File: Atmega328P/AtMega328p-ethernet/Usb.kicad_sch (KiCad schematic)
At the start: 19 parts, among them J2 USB_C_Receptacle_USB2.0_16P, U3 MCP2200-I-SS, Y3 12MHz

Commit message: Most components selected using lcsc
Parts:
- removed C25: 100nF, Capacitor_SMD:C_0603_1608Metric, symbol Device:C_Small
- removed R20: 470R, Resistor_SMD:R_0603_1608Metric, symbol Device:R_Small
- removed U3: MCP2200-I-SS, Package_SO:SSOP-20_5.3x7.2mm_P0.65mm, symbol Interface_USB:MCP2200-I-SS
- added U3: CP2102N-Axx-xQFN28, Package_DFN_QFN:QFN-28-1EP_5x5mm_P0.5mm_EP3.35x3.35mm, symbol Interface_USB:CP2102N-Axx-xQFN28
- D3: value LED -> LED-GREEN; footprint LED_SMD:LED_0603_1608Metric -> LED_SMD:LED_0805_2012Metric; LCSC C2286 -> C2297
- FB2: value HH-1M1608-121JT -> 100R@100MHz; LCSC (none) -> C1015
- J2: value USB_C_Receptacle_USB2.0_16P -> USB_C_Receptacle_USB2.0_12P; LCSC (none) -> C2988369
- R21: value 10k -> 1k
- Y3: footprint Crystal:Crystal_SMD_2012-2Pin_2.0x1.2mm -> Crystal:Crystal_SMD_3225-4Pin_3.2x2.5mm
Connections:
- net USB_P is gone; now on net USB_N: J2.A6 (D+), J2.B6 (D+)
- net +5V: now also U3.6 (VDD)
- net USB_N: now also U3.4 (D+), U3.5 (D-)
- net VBUS: now also U3.8 (VBUS)
- new net: U3.29 (GND), U3.3 (GND)
- no-connect marks 5 -> 4
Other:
- moved on the sheet: C26, C27, FB2, R21, TP1, TP2, TP3, TP4

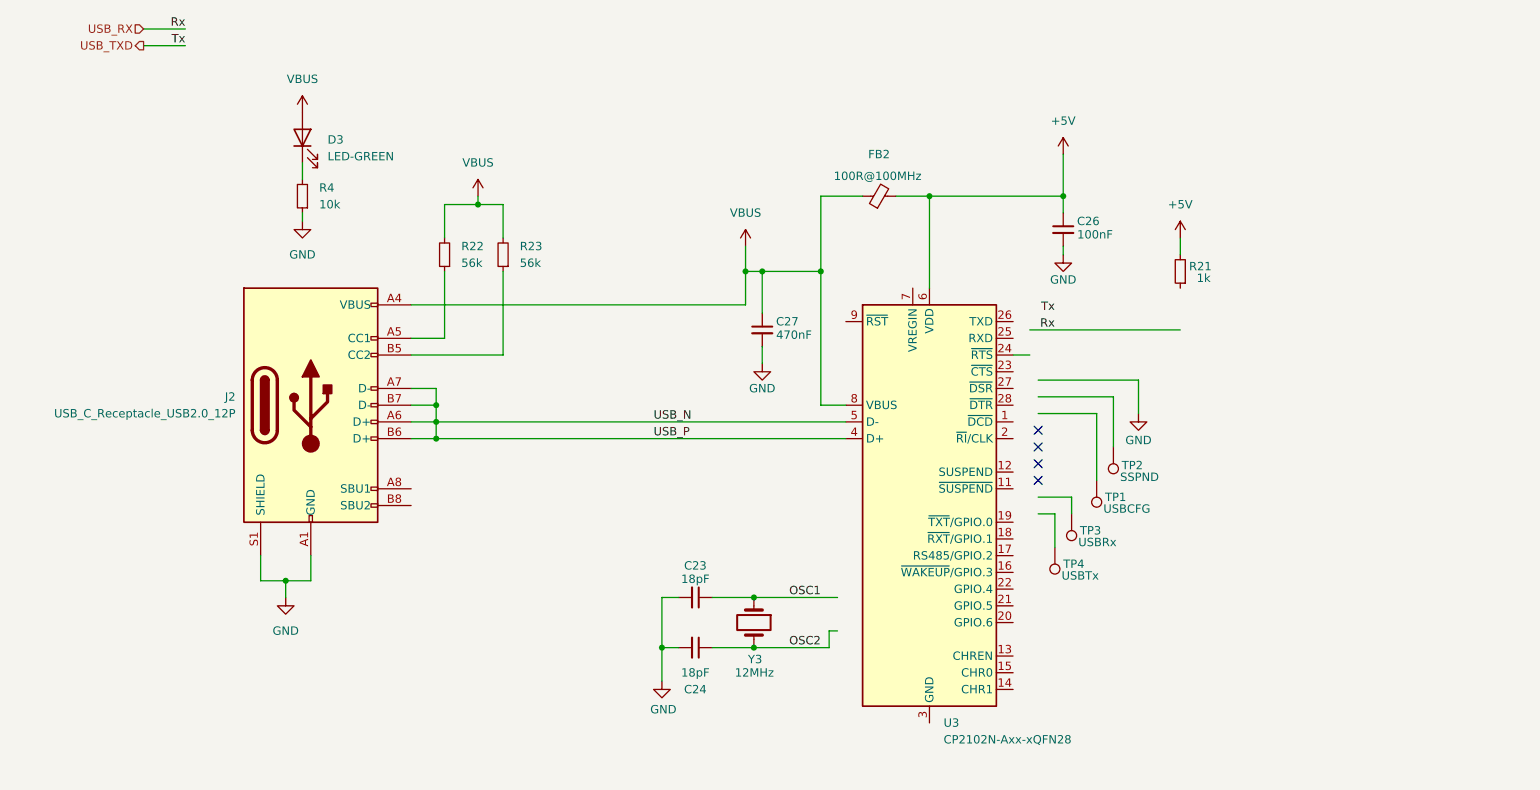
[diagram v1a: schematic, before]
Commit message: All parts matching lcsc replaced usb transever
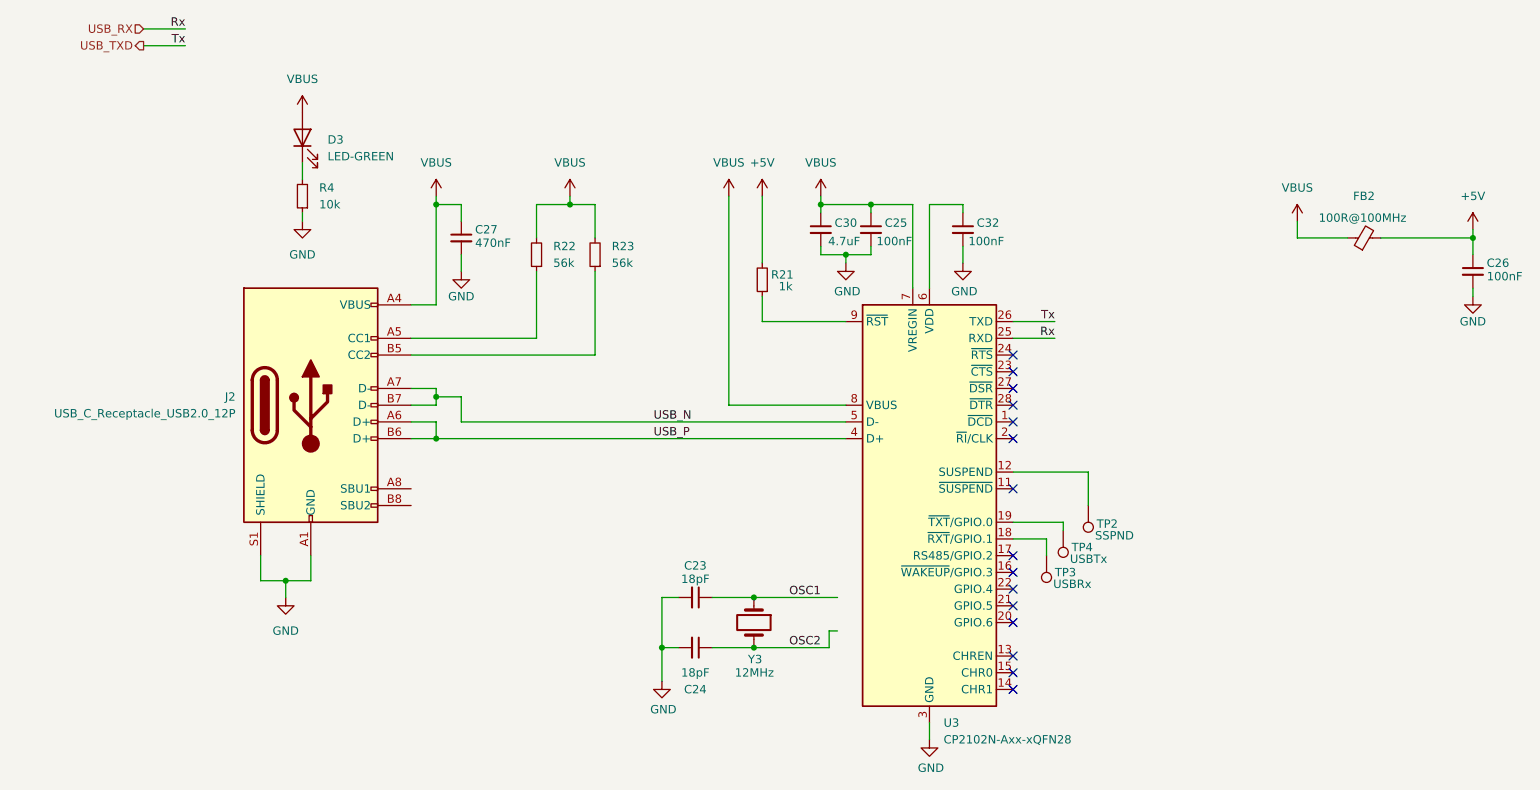
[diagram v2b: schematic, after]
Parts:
- removed TP1: USBCFG, TestPoint:TestPoint_Pad_1.0x1.0mm, symbol Connector:TestPoint
- added C25, C32: 100nF, Capacitor_SMD:C_0603_1608Metric, symbol Device:C_Small
- added C30: 4.7uF, Capacitor_SMD:C_0603_1608Metric, symbol Device:C_Small
- R21: LCSC (none) -> C21190
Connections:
- net +5V: no longer U3.6 (VDD)
- net GND: now also U3.29 (GND), U3.3 (GND), C25.2, C30.2, C32.2
- net USB_N: no longer J2.A6 (D+), J2.B6 (D+), U3.4 (D+)
- net USB_RX: now also U3.25 (RXD)
- net USB_TXD: now also U3.26 (TXD)
- net VBUS: now also U3.7 (VREGIN), C25.1, C30.1
- net at U3.12 (SUSPEND): now also TP2.1
- net at U3.18 (~{RXT}/GPIO.1): now also TP3.1
- net at U3.19 (~{TXT}/GPIO.0): now also TP4.1
- net at U3.9 (~{RST}): now also R21.1
- new net: C32.1, U3.6 (VDD)
- new net USB_P: J2.A6 (D+), J2.B6 (D+), U3.4 (D+)
- no-connect marks 4 -> 15
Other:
- moved on the sheet: C26, C27, FB2, R21, R22, R23, TP2, TP3, TP4

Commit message: Continued cleanup
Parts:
- removed C23, C24: 18pF, Capacitor_SMD:C_0603_1608Metric, symbol Device:C_Small
- removed C26: 100nF, Capacitor_SMD:C_0603_1608Metric, symbol Device:C_Small
- removed FB2: 100R@100MHz, Inductor_SMD:L_0603_1608Metric, symbol Device:FerriteBead_Small
- removed Y3: 12MHz, Crystal:Crystal_SMD_3225-4Pin_3.2x2.5mm, symbol Device:Crystal
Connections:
- net VBUS: no longer C25.1, C27.1, C30.1, J2.A4 (VBUS), J2.A9 (VBUS), J2.B4 (VBUS), J2.B9 (VBUS), R22.2, R23.2, U3.7 (VREGIN), U3.8 (VBUS)
- net +5V renamed VBUS_OUT
- net VBUS_OUT: now also C25.1, C27.1, C30.1, J2.A4 (VBUS), J2.A9 (VBUS), J2.B4 (VBUS), J2.B9 (VBUS), R22.2, R23.2, U3.7 (VREGIN), U3.8 (VBUS)
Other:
- moved on the sheet: R21

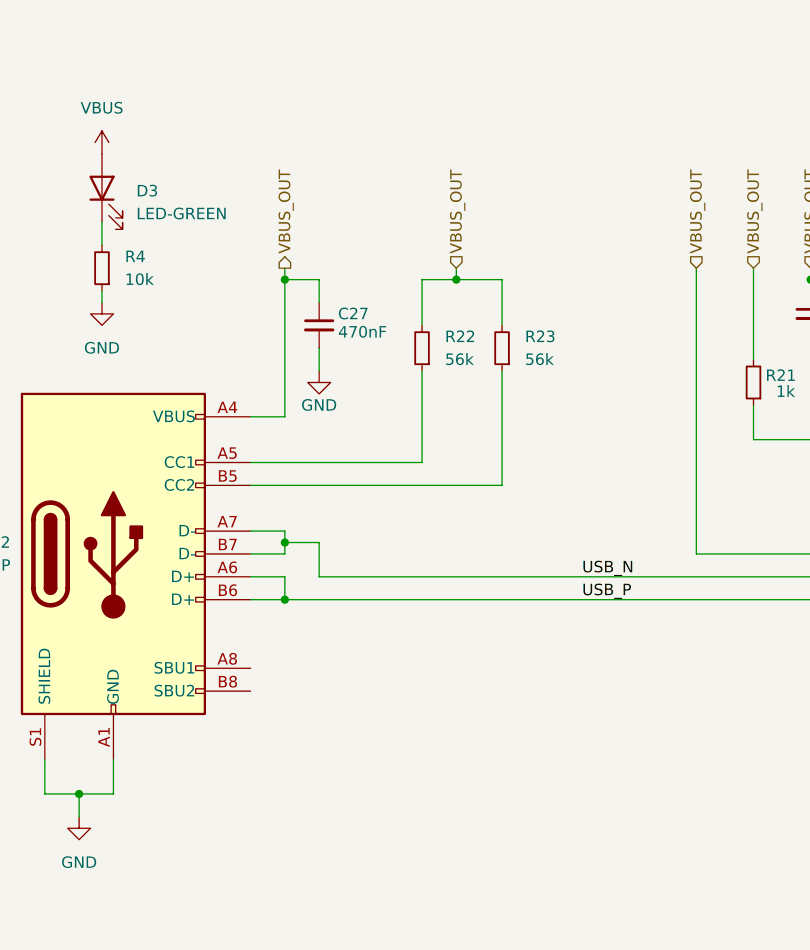
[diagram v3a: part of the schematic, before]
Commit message: USB and microcontroller layed out
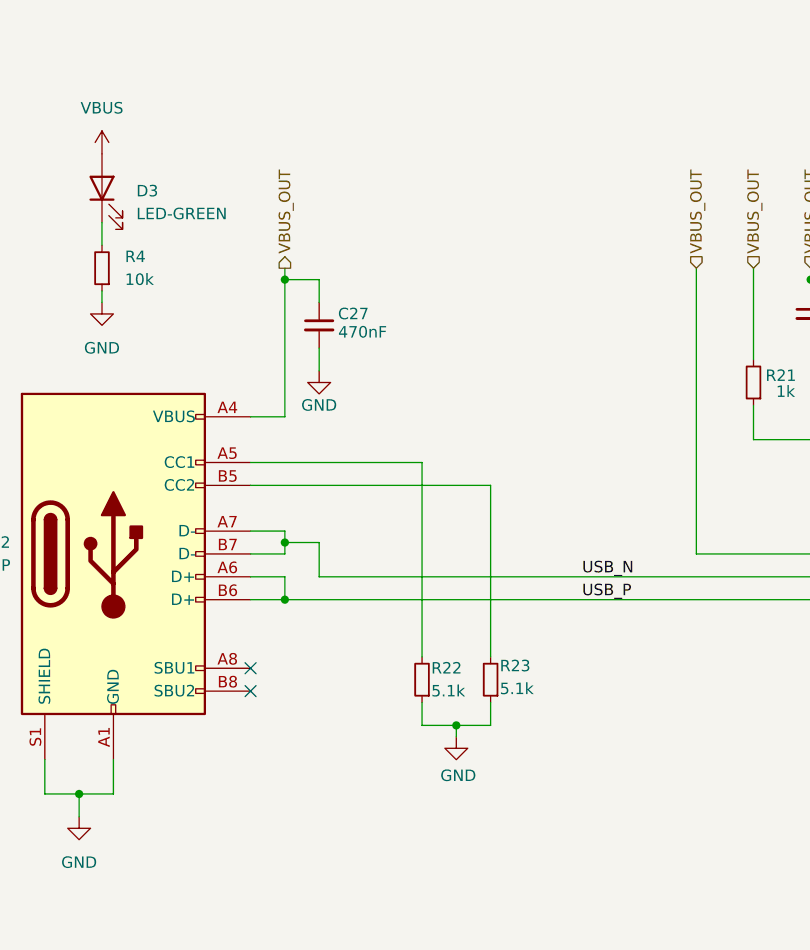
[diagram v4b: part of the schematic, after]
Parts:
- R22: value 56k -> 5.1k; LCSC C23206 -> C23186
- R23: value 56k -> 5.1k; LCSC (none) -> C23186
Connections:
- net GND: now also R22.1, R23.1
- net VBUS_OUT: no longer R22.2, R23.2
- net at J2.B5 (CC2): now also R23.2; no longer R23.1
- net at J2.A5 (CC1): now also R22.2; no longer R22.1
- no-connect marks 15 -> 17
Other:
- moved on the sheet: R22, R23
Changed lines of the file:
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@@
+	)
+	(junction
+		(at 101.6 101.6)
+		(diameter 0)
+		(color 0 0 0 0)
 	)
 	(junction
@@
 		(color 0 0 0 0)
 	)
-	(junction
-		(at 101.6 52.07)
-		(diameter 0)
-		(color 0 0 0 0)
-	)
 	(no_connect
 		(at 170.18 74.93)
@@
 	)
 	(no_connect
+		(at 78.74 95.25)
+	)
+	(no_connect
 		(at 170.18 125.73)
 	)
@@
 	)
 	(no_connect
+		(at 78.74 97.79)
+	)
+	(no_connect
 		(at 170.18 113.03)
 	)
@@
 	(wire
 		(pts
+			(xy 97.79 72.39) (xy 97.79 93.98)
+		)
+		(stroke
+			(width 0)
+			(type default)
+		)
+	)
+	(wire
+		(pts
 			(xy 140.97 59.69) (xy 144.78 59.69)
 		)
@@
 	(wire
 		(pts
-			(xy 78.74 74.93) (xy 106.68 74.93)
+			(xy 78.74 74.93) (xy 105.41 74.93)
 		)
 		(stroke
@@
 	(wire
 		(pts
-			(xy 97.79 52.07) (xy 101.6 52.07)
+			(xy 105.41 101.6) (xy 101.6 101.6)
 		)
 		(stroke
@@
 	(wire
 		(pts
+			(xy 105.41 99.06) (xy 105.41 101.6)
+		)
+		(stroke
+			(width 0)
+			(type default)
+		)
+	)
+	(wire
+		(pts
 			(xy 170.18 72.39) (xy 176.53 72.39)
 		)
@@
 	(wire
 		(pts
+			(xy 97.79 101.6) (xy 101.6 101.6)
+		)
+		(stroke
+			(width 0)
+			(type default)
+		)
+	)
+	(wire
+		(pts
 			(xy 82.55 81.28) (xy 86.36 81.28)
 		)
@@
 	(wire
 		(pts
+			(xy 101.6 101.6) (xy 101.6 102.87)
+		)
+		(stroke
+			(width 0)
+			(type default)
+		)
+	)
+	(wire
+		(pts
 			(xy 140.97 52.07) (xy 148.59 52.07)
 		)
@@
 	(wire
 		(pts
-			(xy 106.68 57.15) (xy 106.68 52.07)
-		)
-		(stroke
-			(width 0)
-			(type default)
-		)
-	)
-	(wire
-		(pts
 			(xy 170.18 100.33) (xy 177.8 100.33)
 		)
@@
 	(wire
 		(pts
+			(xy 105.41 74.93) (xy 105.41 93.98)
+		)
+		(stroke
+			(width 0)
+			(type default)
+		)
+	)
+	(wire
+		(pts
 			(xy 148.59 52.07) (xy 148.59 53.34)
 		)
@@
 	(wire
 		(pts
-			(xy 97.79 72.39) (xy 97.79 62.23)
-		)
-		(stroke
-			(width 0)
-			(type default)
-		)
-	)
-	(wire
-		(pts
 			(xy 82.55 87.63) (xy 144.78 87.63)
 		)
@@
 	(wire
 		(pts
-			(xy 101.6 52.07) (xy 106.68 52.07)
-		)
-		(stroke
-			(width 0)
-			(type default)
-		)
-	)
-	(wire
-		(pts
 			(xy 55.88 105.41) (xy 55.88 109.22)
 		)
@@
 	(wire
 		(pts
-			(xy 97.79 57.15) (xy 97.79 52.07)
-		)
-		(stroke
-			(width 0)
-			(type default)
-		)
-	)
-	(wire
-		(pts
 			(xy 148.59 59.69) (xy 148.59 58.42)
 		)
@@
 	(wire
 		(pts
-			(xy 106.68 74.93) (xy 106.68 62.23)
-		)
-		(stroke
-			(width 0)
-			(type default)
-		)
-	)
-	(wire
-		(pts
 			(xy 82.55 81.28) (xy 82.55 82.55)
 		)
@@
 	(wire
 		(pts
+			(xy 97.79 99.06) (xy 97.79 101.6)
+		)
+		(stroke
+			(width 0)
+			(type default)
+		)
+	)
+	(wire
+		(pts
 			(xy 86.36 85.09) (xy 144.78 85.09)
 		)
@@
 		(pts
 			(xy 162.56 52.07) (xy 162.56 53.34)
-		)
-		(stroke
-			(width 0)
-			(type default)
-		)
-	)
-	(wire
-		(pts
-			(xy 101.6 50.8) (xy 101.6 52.07)
 		)
 		(stroke
@@
 	)
 	(hierarchical_label "VBUS_OUT"
-		(shape input)
-		(at 101.6 50.8 90)
-		(effects
-			(font
-				(size 1.27 1.27)
-			)
-			(justify left)
-		)
-	)
-	(hierarchical_label "VBUS_OUT"
 		(shape output)
 		(at 82.55 50.8 90)
@@
 		(polyline
 			(pts
-				(xy 101.6 83.82) (xy 101.6 88.9) (xy 104.14 88.9) (xy 104.14 83.82)
+				(xy 87.63 83.82) (xy 87.63 88.9) (xy 90.17 88.9) (xy 90.17 83.82)
 			)
 			(stroke
@@
 		(length 2.54)
 		(shape round)
-		(at 102.87 83.82 0)
+		(at 88.9 83.82 0)
 		(fields_autoplaced yes)
 		(effects
@@
 		)
 		(property "Netclass" "USB"
-			(at 103.5685 81.28 0)
+			(at 89.5985 81.28 0)
 			(effects
 				(font
@@
 		)
 		(property "Component Class" ""
-			(at 93.98 34.29 0)
+			(at 80.01 34.29 0)
 			(effects
 				(font
@@
 	)
 	(symbol
+		(lib_id "power:GND")
+		(at 101.6 102.87 0)
+		(unit 1)
+		(exclude_from_sim no)
+		(in_bom yes)
+		(on_board yes)
+		(dnp no)
+		(property "Reference" "#PWR047"
+			(at 101.6 109.22 0)
+			(effects
+				(font
+					(size 1.27 1.27)
+				)
+				(hide yes)
+			)
+		)
+		(property "Value" "GND"
+			(at 99.822 107.188 0)
+			(effects
+				(font
+					(size 1.27 1.27)
+				)
+				(justify left)
+			)
+		)
+		(property "Footprint" ""
+			(at 101.6 102.87 0)
+			(effects
+				(font
+					(size 1.27 1.27)
+				)
+				(hide yes)
+			)
+		)
+		(property "Datasheet" ""
+			(at 101.6 102.87 0)
+			(effects
+				(font
+					(size 1.27 1.27)
+				)
+				(hide yes)
+			)
+		)
+		(property "Description" "Power symbol creates a global label with name \"GND\" , ground"
+			(at 101.6 102.87 0)
+			(effects
+				(font
+					(size 1.27 1.27)
+				)
+				(hide yes)
+			)
+		)
+		(pin "1"
+		)
+		(instances
+			(project "AtMega328p-ethernet"
+				(path "/441f74dc-335f-4227-aefc-792ec34889a2/1cfd0189-4634-4020-adfb-07004d661840"
+					(reference "#PWR047")
+					(unit 1)
+				)
+			)
+		)
+	)
+	(symbol
 		(lib_id "Device:C_Small")
 		(at 140.97 55.88 0)
@@
 	(symbol
 		(lib_id "Device:R_Small")
-		(at 106.68 59.69 180)
+		(at 105.41 96.52 180)
 		(unit 1)
 		(exclude_from_sim no)
@@
 		(on_board yes)
 		(dnp no)
-		(fields_autoplaced yes)
 		(property "Reference" "R23"
-			(at 109.22 58.4199 0)
+			(at 106.426 94.996 0)
 			(effects
 				(font
@@
 			)
 		)
-		(property "Value" "56k"
-			(at 109.22 60.9599 0)
+		(property "Value" "5.1k"
+			(at 106.426 97.536 0)
 			(effects
 				(font
@@
 		)
 		(property "Footprint" "Resistor_SMD:R_0603_1608Metric"
-			(at 106.68 59.69 0)
+			(at 105.41 96.52 0)
 			(effects
 				(font
@@
 		)
 		(property "Datasheet" "~"
-			(at 106.68 59.69 0)
+			(at 105.41 96.52 0)
 			(effects
 				(font
@@
 		)
 		(property "Description" "Resistor, small symbol"
-			(at 106.68 59.69 0)
+			(at 105.41 96.52 0)
+			(effects
+				(font
+					(size 1.27 1.27)
+				)
+				(hide yes)
+			)
+		)
+		(property "LCSC" "C23186"
+			(at 105.41 96.52 0)
 			(effects
 				(font
@@
 	(symbol
 		(lib_id "Device:R_Small")
-		(at 97.79 59.69 180)
+		(at 97.79 96.52 180)
 		(unit 1)
 		(exclude_from_sim no)
@@
 		(on_board yes)
 		(dnp no)
-		(fields_autoplaced yes)
 		(property "Reference" "R22"
-			(at 100.33 58.4199 0)
+			(at 98.806 95.25 0)
 			(effects
 				(font
@@
 			)
 		)
-		(property "Value" "56k"
-			(at 100.33 60.9599 0)
+		(property "Value" "5.1k"
+			(at 98.806 97.79 0)
 			(effects
 				(font
@@
 		)
 		(property "Footprint" "Resistor_SMD:R_0603_1608Metric"
-			(at 97.79 59.69 0)
+			(at 97.79 96.52 0)
 			(effects
 				(font
@@
 		)
 		(property "Datasheet" "~"
-			(at 97.79 59.69 0)
+			(at 97.79 96.52 0)
 			(effects
 				(font
@@
 		)
 		(property "Description" "Resistor, small symbol"
-			(at 97.79 59.69 0)
-			(effects
-				(font
-					(size 1.27 1.27)
-				)
-				(hide yes)
-			)
-		)
-		(property "LCSC" "C23206"
-			(at 97.79 59.69 0)
-			(effects
-				(font
+			(at 97.79 96.52 0)
+			(effects
+				(font
+					(size 1.27 1.27)
+				)
+				(hide yes)
+			)
+		)
+		(property "LCSC" "C23186"
+			(at 97.79 96.52 0)
+			(effects
+				(font

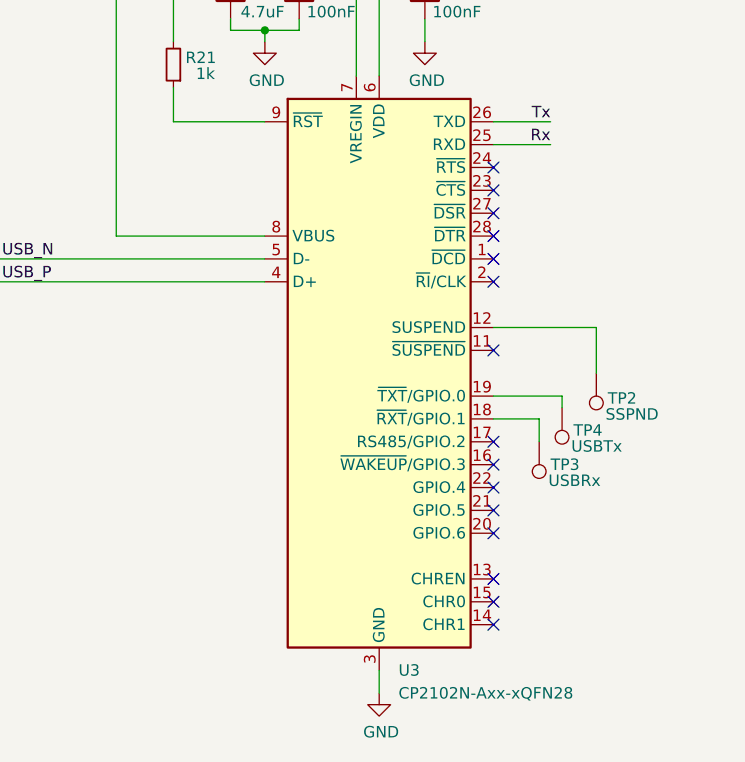
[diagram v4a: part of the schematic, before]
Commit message: Most components layed out and locked still to do ethernet
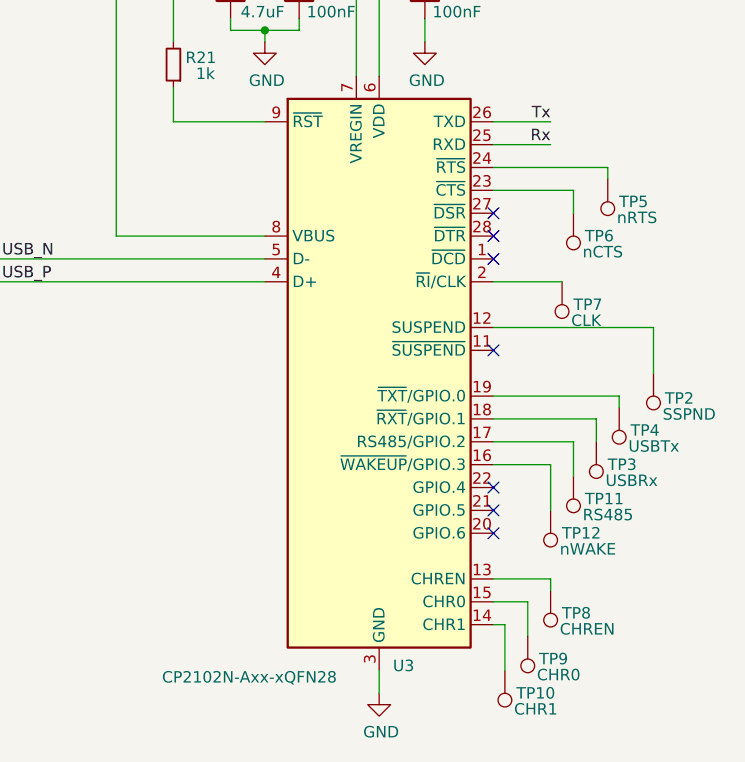
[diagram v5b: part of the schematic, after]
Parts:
- added TP10: CHR1, TestPoint:TestPoint_Pad_1.0x1.0mm, symbol Connector:TestPoint
- added TP11: RS485, TestPoint:TestPoint_Pad_1.0x1.0mm, symbol Connector:TestPoint
- added TP12: nWAKE, TestPoint:TestPoint_Pad_1.0x1.0mm, symbol Connector:TestPoint
- added TP5: nRTS, TestPoint:TestPoint_Pad_1.0x1.0mm, symbol Connector:TestPoint
- added TP6: nCTS, TestPoint:TestPoint_Pad_1.0x1.0mm, symbol Connector:TestPoint
- added TP7: CLK, TestPoint:TestPoint_Pad_1.0x1.0mm, symbol Connector:TestPoint
- added TP8: CHREN, TestPoint:TestPoint_Pad_1.0x1.0mm, symbol Connector:TestPoint
- added TP9: CHR0, TestPoint:TestPoint_Pad_1.0x1.0mm, symbol Connector:TestPoint
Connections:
- net at U3.13 (CHREN): now also TP8.1
- net at U3.14 (CHR1): now also TP10.1
- net at U3.15 (CHR0): now also TP9.1
- net at U3.16 (~{WAKEUP}/GPIO.3): now also TP12.1
- net at U3.17 (RS485/GPIO.2): now also TP11.1
- net at U3.2 (~{RI}/CLK): now also TP7.1
- net at U3.23 (~{CTS}): now also TP6.1
- net at U3.24 (~{RTS}): now also TP5.1
- no-connect marks 17 -> 9
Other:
- moved on the sheet: TP2, TP3, TP4
